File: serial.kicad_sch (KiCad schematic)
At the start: 57 parts, among them J1001 RX Sel Header, J1002 Terminal Block Socket, J1003 Terminal Block Socket, J1004 Terminal Block Socket, J1005 Terminal Block Socket, U1001 SN75176BDR, U1002 74LVC2G17, U1003 SP3232EEY-L/TR, U1004 SN75176BDR

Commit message: WIP wiring
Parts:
- FL1001, FL1002: footprint PCM_Ferrite_SMD_AKL:Ferrite_0805_2012Metric -> HALSER:L_CommonModeChoke_PCAQ2012B; symbol Device:Filter_EMI_CommonMode -> Device:L_Ferrite_Coupled_1243
- J1002: value Terminal Block Socket -> RS485 RX Socket
- J1003: value Terminal Block Socket -> RS485 TX Socket
- J1004: value Terminal Block Socket -> RS-232 Socket
- J1005: value Terminal Block Socket -> UART Socket
- U1001, U1004: footprint Package_SO:SOIC-8_3.9x4.9mm_P1.27mm -> PCM_Package_SO_AKL:SOIC-8_3.9x4.9mm_P1.27mm
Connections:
- net RS485_RX: now also J1001.6 (Pin_6); no longer J1001.2 (Pin_2)
- net RS485_RX_A_LINE: now also D1003.2 (A2); no longer D1003.1 (A1)
- net RS485_RX_B_LINE: now also D1003.1 (A1), FL1001.3; no longer D1003.2 (A2), FL1001.4
- net UART_RX: now also J1001.2 (Pin_2); no longer J1001.6 (Pin_6)
- net at C1010.1, R1006.2: now also FL1001.4; no longer FL1001.3
- net at D1004.2 (A2), D1006.1 (A1), F1004.2: now also FL1002.3; no longer FL1002.4
- net at C1011.1, R1008.2: now also FL1002.4; no longer FL1002.3
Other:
- note removed: "NMEA 0183 RX"
- note removed: "NMEA 0183 TX"

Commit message: Further design adjustments
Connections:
- net UART_RX_C: now reaches C1015.1, D1009.2 (A2), FB1002.2, J1005.2 (Pin_2)
- net UART_TX_C: now reaches C1014.1, D1007.2 (A2), FB1001.2, J1005.3 (Pin_3)
- net RS232_RX_LINE renamed RS232_RX_C
- net RS232_TX_LINE renamed RS232_TX_C
- net RS485_RX_A_LINE renamed RS485_RX_B_C
- net RS485_RX_B_LINE renamed RS485_RX_A_C
- net RS485_TX_A_LINE renamed RS485_TX_A_C
- net RS485_TX_B_LINE renamed RS485_TX_B_C
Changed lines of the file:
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@@
 		)
 	)
-	(label "RS485_TX_B_LINE"
+	(label "RS485_TX_B_C"
 		(at 248.92 73.66 180)
 		(fields_autoplaced yes)
@@
 		)
 	)
-	(label "RS232_TX_LINE"
+	(label "UART_RX_C"
+		(at 240.03 147.32 0)
+		(fields_autoplaced yes)
+		(effects
+			(font
+				(size 1.27 1.27)
+			)
+			(justify left bottom)
+		)
+	)
+	(label "UART_TX_C"
+		(at 240.03 144.78 0)
+		(fields_autoplaced yes)
+		(effects
+			(font
+				(size 1.27 1.27)
+			)
+			(justify left bottom)
+		)
+	)
+	(label "RS232_TX_C"
 		(at 256.54 100.33 180)
 		(fields_autoplaced yes)
@@
 		)
 	)
-	(label "RS485_RX_B_LINE"
-		(at 232.41 41.91 0)
+	(label "RS485_RX_B_C"
+		(at 232.41 21.59 0)
 		(fields_autoplaced yes)
 		(effects
@@
 		)
 	)
-	(label "RS485_TX_A_LINE"
+	(label "RS485_TX_A_C"
 		(at 251.46 52.07 180)
 		(fields_autoplaced yes)
@@
 		)
 	)
-	(label "RS232_RX_LINE"
+	(label "RS232_RX_C"
 		(at 256.54 102.87 180)
 		(fields_autoplaced yes)
@@
 		)
 	)
-	(label "RS485_RX_A_LINE"
-		(at 232.41 21.59 180)
-		(fields_autoplaced yes)
-		(effects
-			(font
-				(size 1.27 1.27)
-			)
-			(justify right bottom)
-		)
-	)
+	(label "RS485_RX_A_C"
+		(at 232.41 41.91 0)
+		(fields_autoplaced yes)
+		(effects
+			(font
+				(size 1.27 1.27)
+			)
+			(justify left bottom)
+		)
+	)

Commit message: Further manufacturing tweaks
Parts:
- D1003, D1004, D1008: JLCPCB_CORRECTION (none) -> 0;0;180
- J1001: JLCPCB_CORRECTION (none) -> 1.27;2.54;90
- J1002, J1003, J1004, J1005: JLCPCB_CORRECTION (none) -> 3.81;0;180
- U1001, U1002, U1003, U1004: JLCPCB_CORRECTION (none) -> 0;0;270
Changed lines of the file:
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@@
 			)
 		)
+		(property "JLCPCB_CORRECTION" "0;0;180"
+			(at 217.17 69.85 0)
+			(effects
+				(font
+					(size 1.27 1.27)
+				)
+				(hide yes)
+			)
+		)
 		(pin "3"
 		)
@@
 			)
 		)
+		(property "JLCPCB_CORRECTION" "3.81;0;180"
+			(at 261.62 147.32 0)
+			(effects
+				(font
+					(size 1.27 1.27)
+				)
+				(hide yes)
+			)
+		)
 		(pin "3"
 		)
@@
 			)
 		)
+		(property "JLCPCB_CORRECTION" "0;0;180"
+			(at 236.22 113.03 0)
+			(effects
+				(font
+					(size 1.27 1.27)
+				)
+				(hide yes)
+			)
+		)
 		(pin "3"
 		)
@@
 			)
 		)
+		(property "JLCPCB_CORRECTION" "1.27;2.54;90"
+			(at 35.56 106.68 0)
+			(effects
+				(font
+					(size 1.27 1.27)
+				)
+				(hide yes)
+			)
+		)
 		(pin "2"
 		)
@@
 			)
 		)
+		(property "JLCPCB_CORRECTION" "0;0;270"
+			(at 115.57 176.53 0)
+			(effects
+				(font
+					(size 1.27 1.27)
+				)
+				(hide yes)
+			)
+		)
 		(pin "5"
 		)
@@
 			)
 		)
+		(property "JLCPCB_CORRECTION" "0;0;270"
+			(at 80.01 44.45 0)
+			(effects
+				(font
+					(size 1.27 1.27)
+				)
+				(hide yes)
+			)
+		)
 		(pin "7"
 		)
@@
 			)
 		)
+		(property "JLCPCB_CORRECTION" "3.81;0;180"
+			(at 261.62 33.02 0)
+			(effects
+				(font
+					(size 1.27 1.27)
+				)
+				(hide yes)
+			)
+		)
 		(pin "3"
 		)
@@
 			)
 		)
+		(property "JLCPCB_CORRECTION" "0;0;270"
+			(at 118.11 168.91 0)
+			(effects
+				(font
+					(size 1.27 1.27)
+				)
+				(hide yes)
+			)
+		)
 		(pin "5"
 		)
@@
 			)
 		)
+		(property "JLCPCB_CORRECTION" "0;0;270"
+			(at 121.92 44.45 0)
+			(effects
+				(font
+					(size 1.27 1.27)
+				)
+				(hide yes)
+			)
+		)
 		(pin "7"
 		)
@@
 			)
 		)
+		(property "JLCPCB_CORRECTION" "3.81;0;180"
+			(at 261.62 62.23 0)
+			(effects
+				(font
+					(size 1.27 1.27)
+				)
+				(hide yes)
+			)
+		)
 		(pin "3"
 		)
@@
 			)
 		)
+		(property "JLCPCB_CORRECTION" "0;0;180"
+			(at 217.17 40.64 0)
+			(effects
+				(font
+					(size 1.27 1.27)
+				)
+				(hide yes)
+			)
+		)
 		(pin "3"
 		)
@@
 			)
 		)
+		(property "JLCPCB_CORRECTION" "0;0;270"
+			(at 101.6 107.95 0)
+			(effects
+				(font
+					(size 1.27 1.27)
+				)
+				(hide yes)
+			)
+		)
 		(pin "12"
 		)
@@
 			)
 		)
+		(property "JLCPCB_CORRECTION" "0;0;270"
+			(at 83.82 176.53 0)
+			(effects
+				(font
+					(size 1.27 1.27)
+				)
+				(hide yes)
+			)
+		)
 		(pin "5"
 		)
@@
 			(at 261.62 102.87 0)
 			(effects
+				(font
+					(size 1.27 1.27)
+				)
+				(hide yes)
+			)
+		)
+		(property "JLCPCB_CORRECTION" "3.81;0;180"
+			(at 261.62 102.87 0)
+			(effects

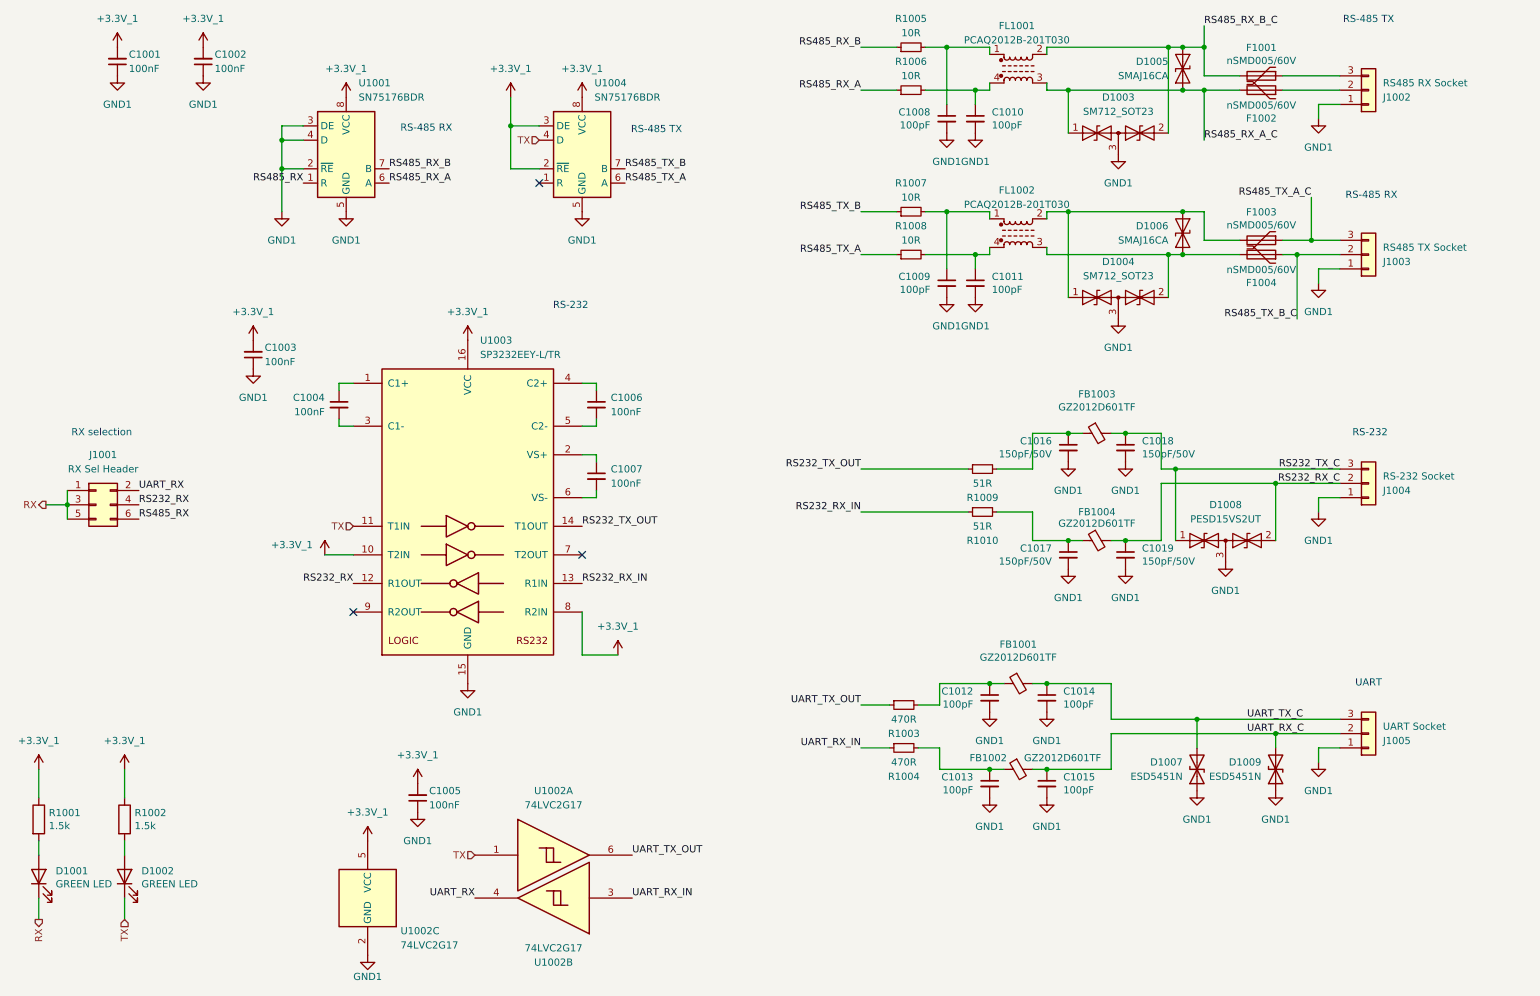
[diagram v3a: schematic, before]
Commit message: Fix issues found in -a1
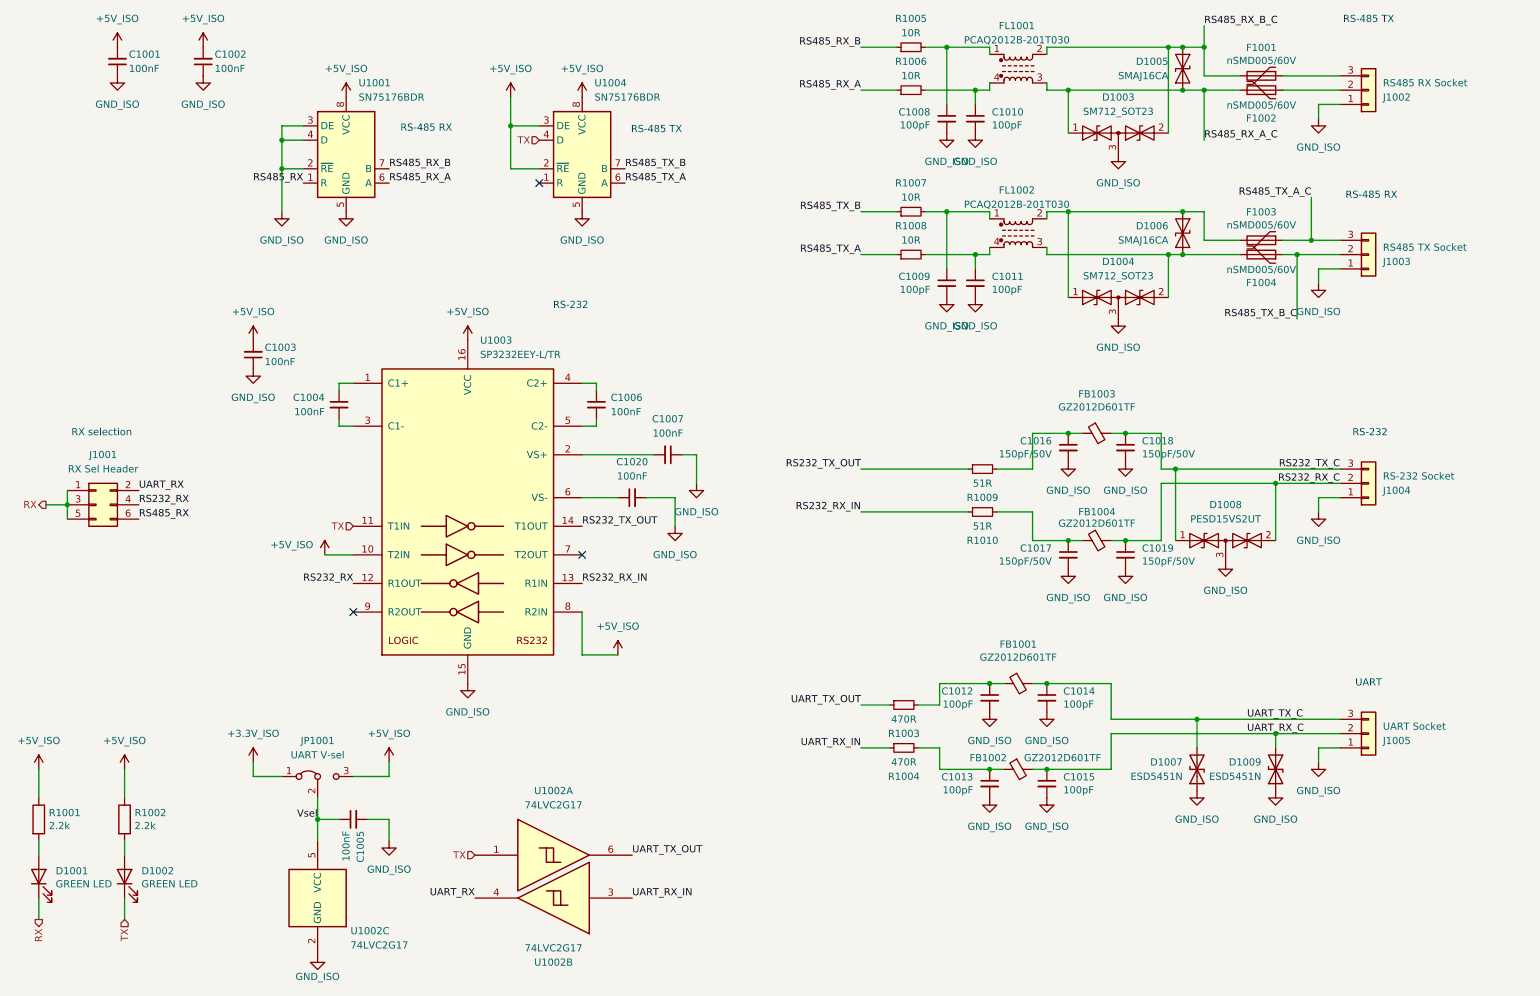
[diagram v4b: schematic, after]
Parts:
- added C1020: 100nF, Capacitor_SMD:C_0402_1005Metric, symbol Device:C_Small
- added JP1001: UART V-sel, Connector_PinHeader_2.54mm:PinHeader_1x03_P2.54mm_Vertical, symbol Jumper:Jumper_3_Bridged12
- C1001, C1002, C1003, C1004, C1005, C1006, C1007: footprint PCM_Capacitor_SMD_AKL:C_0402_1005Metric -> Capacitor_SMD:C_0402_1005Metric
- C1008, C1009, C1010, C1011, C1012, C1013, C1014, C1015, C1016, C1017, C1018, C1019: footprint PCM_Capacitor_SMD_AKL:C_0603_1608Metric -> Capacitor_SMD:C_0603_1608Metric
- D1001, D1002: footprint PCM_LED_SMD_AKL:LED_0603_1608Metric -> LED_SMD:LED_0603_1608Metric
- D1003, D1004, D1008: footprint PCM_Package_TO_SOT_SMD_AKL:SOT-23 -> Package_TO_SOT_SMD:SOT-23
- D1005, D1006: footprint PCM_Diode_SMD_AKL:D_SMA_TVS -> Diode_SMD:D_SMA
- D1007, D1009: footprint PCM_Diode_SMD_AKL:D_0402_1005Metric -> Diode_SMD:D_0402_1005Metric
- F1001, F1002, F1003, F1004: footprint PCM_Fuse_AKL:Fuse_1206_3216Metric -> Fuse:Fuse_1206_3216Metric
- FB1001, FB1002, FB1003, FB1004: footprint PCM_Ferrite_SMD_AKL:Ferrite_0805_2012Metric -> Inductor_SMD:L_0805_2012Metric
- R1001, R1002: value 1.5k -> 2.2k; footprint PCM_Resistor_SMD_AKL:R_0402_1005Metric -> Resistor_SMD:R_0402_1005Metric; LCSC C25867 -> (none)
- R1003, R1004, R1005, R1006, R1007, R1008: footprint PCM_Resistor_SMD_AKL:R_0402_1005Metric -> Resistor_SMD:R_0402_1005Metric
- R1009, R1010: footprint PCM_Resistor_SMD_AKL:R_0603_1608Metric -> Resistor_SMD:R_0603_1608Metric
- U1001, U1004: footprint PCM_Package_SO_AKL:SOIC-8_3.9x4.9mm_P1.27mm -> Package_SO:SOIC-8_3.9x4.9mm_P1.27mm
- U1002: footprint PCM_Package_TO_SOT_SMD_AKL:SOT-23-6 -> Package_TO_SOT_SMD:SOT-23-6
- U1003: footprint PCM_Package_SO_AKL:TSSOP-16_4.4x5mm_P0.65mm -> Package_SO:TSSOP-16_4.4x5mm_P0.65mm
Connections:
- net at U1003.2 (VS+): now also C1007.2; no longer C1007.1
- net at U1003.6 (VS-): now also C1020.1; no longer C1007.2
- net +3.3V_1 renamed +5V_ISO
- net +5V_ISO: now also JP1001.3 (B); no longer C1005.2, U1002.5 (VCC)
- net GND1 renamed GND_ISO
- net GND_ISO: now also C1005.2, C1007.1, C1020.2; no longer C1005.1
- new net +3.3V_ISO: JP1001.1 (A)
- new net Vsel: C1005.1, JP1001.2 (C), U1002.5 (VCC)
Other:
- company: Hat Labs Ltd -> Hat Labs oy
- title: Hat Labs Marine Engine & Tank interface (HALMET) -> Hat Labs Serial Interface Device (HALSER)
- moved on the sheet: C1005, C1007, U1002C

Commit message: Bump versions
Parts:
- R1009: renamed from R1003; footprint Resistor_SMD:R_0402_1005Metric -> Resistor_SMD:R_0603_1608Metric; LCSC C25117 -> C23179
- R1010: renamed from R1004; footprint Resistor_SMD:R_0402_1005Metric -> Resistor_SMD:R_0603_1608Metric; LCSC C25117 -> C23179
- renumbered C1020 to C1007, C1007 to C1008, C1008 to C1009, C1009 to C1010, C1012 to C1011, C1013 to C1012, C1016 to C1013, C1017 to C1014, C1010 to C1015, C1011 to C1016, C1014 to C1017, C1015 to C1018, C1018 to C1019, C1019 to C1020, D1008 to D1005, D1007 to D1006, D1005 to D1007, D1006 to D1008, R1005 to R1003, R1006 to R1004, R1007 to R1005, R1008 to R1006, R1009 to R1007, R1010 to R1008, U1002 to U1001, U1001 to U1002
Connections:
- net RS232_RX_C: now also R1008.2; no longer C1020.1, D1005.2 (A2), FB1004.2
- net RS232_RX_IN: now also C1014.1, FB1004.1; no longer R1008.1
- net RS232_TX_C: now also R1007.2; no longer C1019.1, D1005.1 (A1), FB1003.2
- net RS232_TX_OUT: now also C1013.1, FB1003.1; no longer R1007.1
- net RS485_RX_A_C: now also F1002.1, J1002.2 (Pin_2); no longer D1003.1 (A1), D1007.1 (A1), F1002.2, FL1001.3
- net RS485_RX_B_C: now also F1001.1, J1002.3 (Pin_3); no longer D1003.2 (A2), D1007.2 (A2), F1001.2, FL1001.2
- net UART_RX_C: now also R1010.2; no longer C1018.1, D1009.2 (A2), FB1002.2
- net UART_RX_IN: now also C1012.1, FB1002.1; no longer R1010.1
- net UART_TX_C: now also R1009.2; no longer C1017.1, D1006.2 (A2), FB1001.2
- net UART_TX_OUT: now also C1011.1, FB1001.1; no longer R1009.1
- new net: D1003.1 (A1), D1007.2 (A2), F1001.2, FL1001.2
- new net: D1003.2 (A2), D1007.1 (A1), F1002.2, FL1001.3
- new net: C1018.1, D1009.2 (A2), FB1002.2, R1010.1
- new net: C1019.1, D1005.1 (A1), FB1003.2, R1007.1
- new net: C1020.1, D1005.2 (A2), FB1004.2, R1008.1
- new net: C1017.1, D1006.2 (A2), FB1001.2, R1009.1
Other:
- moved on the sheet: C1011, C1012, C1013, C1014, C1017, C1018, C1019, C1020, D1005, D1006, D1009, F1001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
